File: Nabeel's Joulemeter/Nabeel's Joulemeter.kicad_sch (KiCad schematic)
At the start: 54 parts, among them J1 430450200, J3 22035035, J4 22035035, J5 430450200, U1 INA181A1QDBVRQ1, U2 PADS131M04QPWRQ1, U3 UA78M05QDCYRG4Q1, U4 MCP6286T-E/OT

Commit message: LFG BOARD DONE FR
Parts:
- added C12, C13: 4.7uF, 100V, SMV_Passives:CAP_C2220C_2S_KEM, symbol SMV_Custom:C2220C475M1R2C7186
- TP1, TP10, TP11, TP12, TP13, TP14, TP15, TP16, TP17, TP18, TP2, TP3, TP4, TP5, TP6, TP7, TP8, TP9: footprint TestPoint:TestPoint_Pad_D2.0mm -> TestPoint:TestPoint_Pad_D1.0mm
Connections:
- net +12V: now also C12.1
- net GND: now also C12.2, C13.2
- net SHUNT_TO_LOAD: now also C13.1
- net CAN_H renamed CAN_P
- net CAN_L renamed CAN_N

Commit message: made some changes
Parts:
- added H1, H2, H3, H4: MountingHole, MountingHole:MountingHole_5mm, symbol Mechanical:MountingHole

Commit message: almost final
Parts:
- H1, H2, H3, H4: footprint MountingHole:MountingHole_5mm -> MountingHole:MountingHole_3.2mm_M3
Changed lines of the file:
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@@
 			)
 		)
-		(property "Footprint" "MountingHole:MountingHole_5mm"
+		(property "Footprint" "MountingHole:MountingHole_3.2mm_M3"
 			(at 175.26 24.13 0)
 			(effects
@@
 			)
 		)
-		(property "Footprint" "MountingHole:MountingHole_5mm"
+		(property "Footprint" "MountingHole:MountingHole_3.2mm_M3"
 			(at 185.42 40.64 0)
 			(effects
@@
 			)
 		)
-		(property "Footprint" "MountingHole:MountingHole_5mm"
+		(property "Footprint" "MountingHole:MountingHole_3.2mm_M3"
 			(at 180.2881 33.9955 0)
 			(effects
@@
 			)
 		)
-		(property "Footprint" "MountingHole:MountingHole_5mm"
+		(property "Footprint" "MountingHole:MountingHole_3.2mm_M3"
 			(at 190.5 46.99 0)
 			(effects

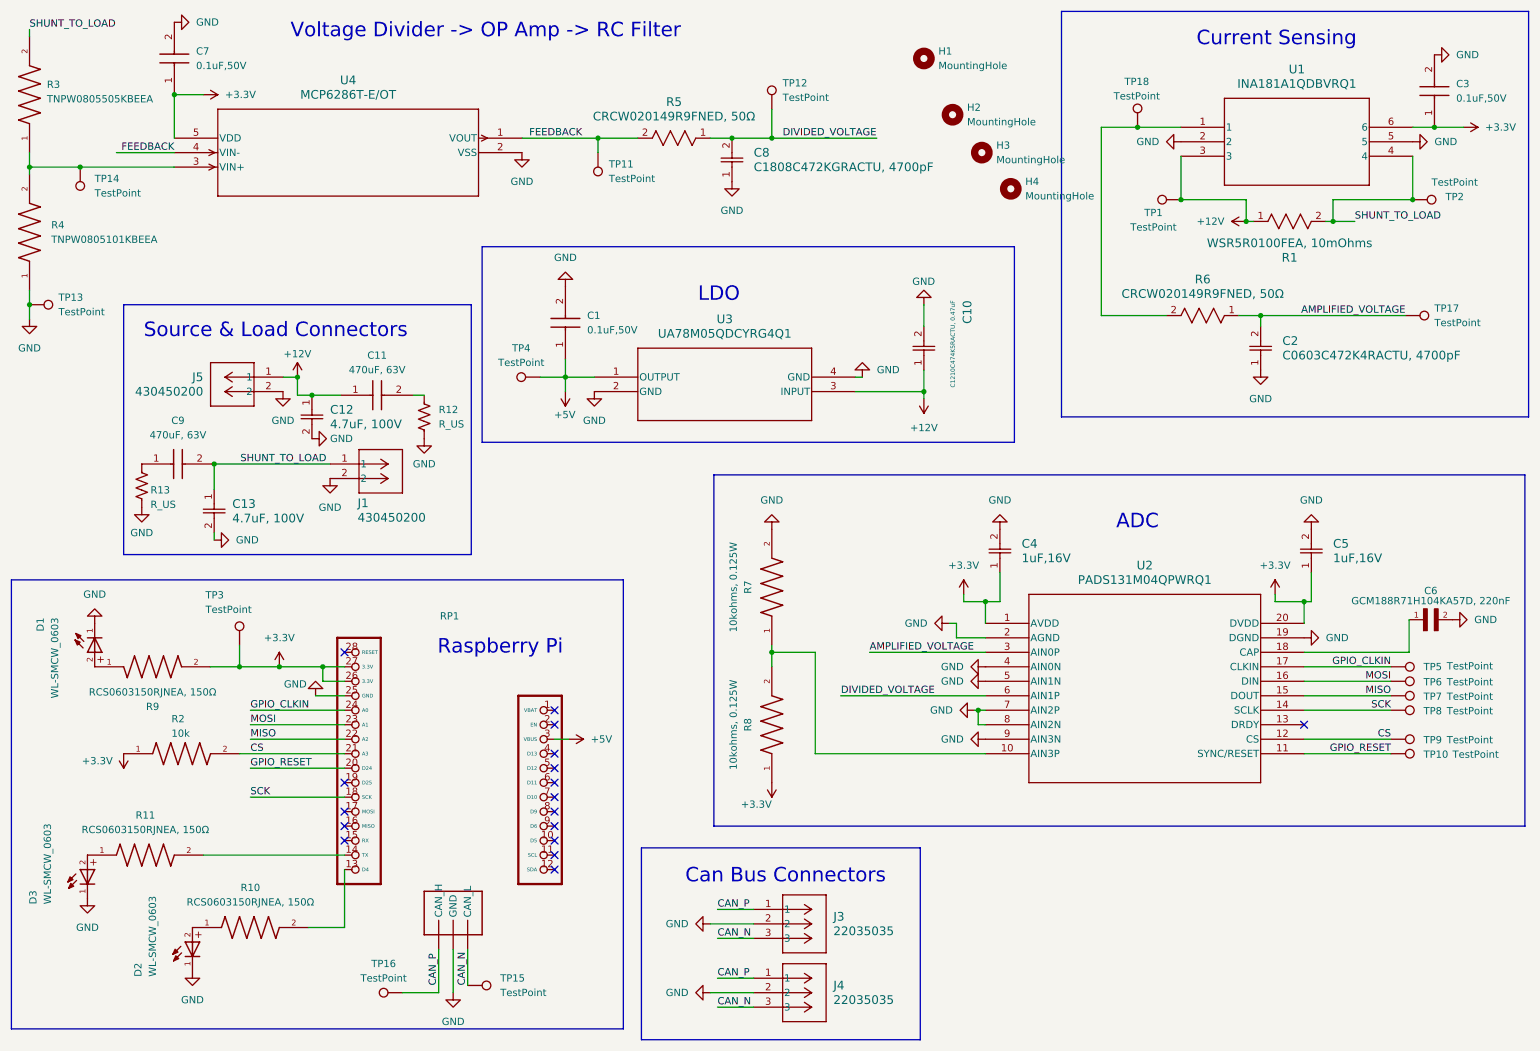
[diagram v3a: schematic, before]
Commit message: Replaced several componentes
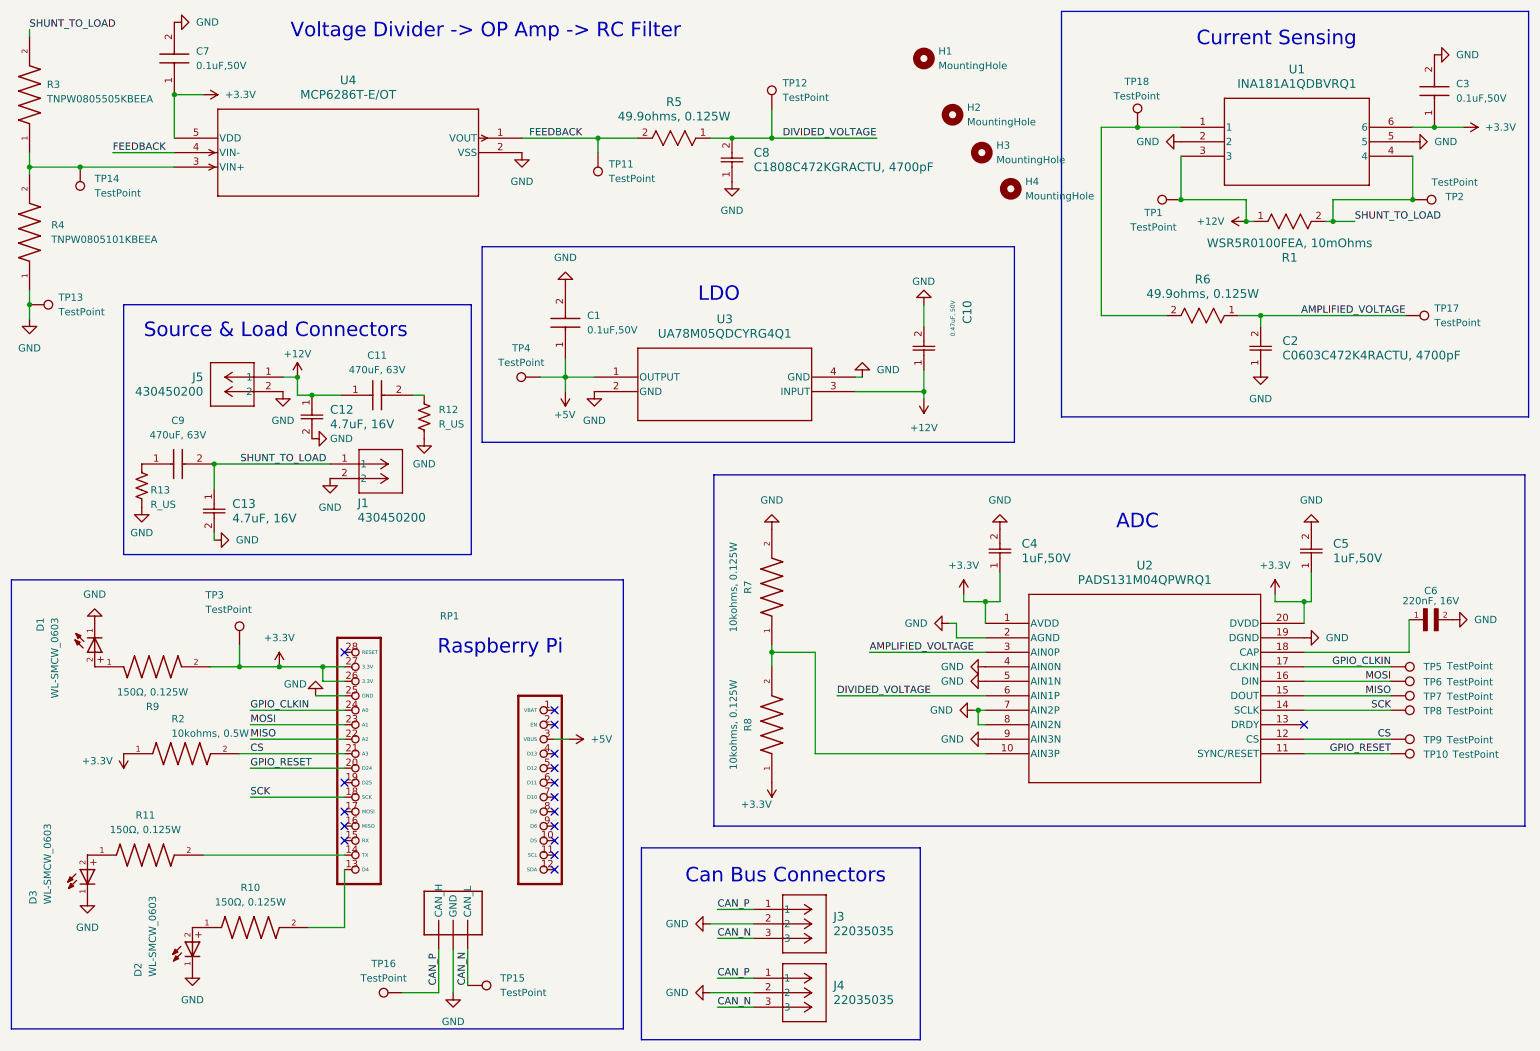
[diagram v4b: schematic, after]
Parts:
- C10: value C1210C474K5RACTU, 0.47uF -> 0.47uF, 50V
- C12, C13: value 4.7uF, 100V -> 4.7uF, 16V; footprint SMV_Passives:CAP_C2220C_2S_KEM -> SMV_Passives:RES_TNPW0805_VIS
- C4, C5: value 1uF,16V -> 1uF,50V
- C6: value GCM188R71H104KA57D, 220nF -> 220nF, 16V
- R10, R11, R9: value RCS0603150RJNEA, 150Ω -> 150Ω, 0.125W
- R2: value 10k -> 10kohms, 0.5W
- R5, R6: value CRCW020149R9FNED, 50Ω -> 49.9ohms, 0.125W
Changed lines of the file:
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@@
 	(wire
 		(pts
-			(xy 33.655 40.64) (xy 43.815 40.64)
-		)
-		(stroke
-			(width 0)
-			(type default)
-		)
-	)
-	(wire
-		(pts
 			(xy 245.745 52.705) (xy 247.015 52.705)
 		)
@@
 	(wire
 		(pts
+			(xy 160.02 135.89) (xy 186.055 135.89)
+		)
+		(stroke
+			(width 0)
+			(type default)
+		)
+	)
+	(wire
+		(pts
 			(xy 145.415 175.895) (xy 137.795 175.895)
 		)
@@
 	(wire
 		(pts
-			(xy 160.655 135.89) (xy 186.055 135.89)
-		)
-		(stroke
-			(width 0)
-			(type default)
-		)
-	)
-	(wire
-		(pts
 			(xy 230.505 69.215) (xy 234.315 69.215)
 		)
@@
 	(wire
 		(pts
+			(xy 33.02 40.64) (xy 43.815 40.64)
+		)
+		(stroke
+			(width 0)
+			(type default)
+		)
+	)
+	(wire
+		(pts
 			(xy 182.245 119.38) (xy 182.245 118.11)
 		)
@@
 	)
 	(label "FEEDBACK"
-		(at 43.815 40.64 180)
+		(at 33.02 40.64 0)
 		(fields_autoplaced yes)
 		(effects
@@
 				(size 1.27 1.27)
 			)
-			(justify right bottom)
+			(justify left bottom)
 		)
 	)
@@
 	)
 	(label "DIVIDED_VOLTAGE"
-		(at 177.165 135.89 180)
+		(at 160.02 135.89 0)
 		(fields_autoplaced yes)
 		(effects
@@
 				(size 1.27 1.27)
 			)
-			(justify right bottom)
+			(justify left bottom)
 		)
 	)
@@
 			)
 		)
-		(property "Value" "GCM188R71H104KA57D, 220nF"
+		(property "Value" "220nF, 16V"
 			(at 264.16 119.253 0)
 			(effects
@@
 			)
 		)
-		(property "Datasheet" ""
+		(property "Datasheet" "C0805C224K5RACAUTO"
 			(at 262.89 122.555 0)
 			(effects
@@
 			)
 		)
-		(property "Description" ""
+		(property "Description" "C129652"
 			(at 262.89 122.555 0)
 			(effects
@@
 			)
 		)
-		(property "Datasheet" "https://content.kemet.com/datasheets/KEM_C1002_X7R_SMD.pdf"
+		(property "Datasheet" "C0805F104K5RACAUTO"
 			(at 460.985 27.305 0)
 			(effects
@@
 			)
 		)
-		(property "Description" "SMD Comm X7R, Ceramic, 0.1 uF, 10%, 50 VDC, 125 VDC, 125C, -55C, X7R, SMD, MLCC, Temperature Stable, Class II, 2.5 % , 5 GOhms, 11 mg, 0805, 2mm, 1.25mm, 0.78mm, 0.75mm, 0.5mm, 4000, 78  Weeks, 80"
+		(property "Description" "C141162"
 			(at 264.795 36.195 0)
 			(effects
@@
 			)
 		)
-		(property "Value" "RCS0603150RJNEA, 150Ω"
+		(property "Value" "150Ω, 0.125W"
 			(at 38.735 159.385 0)
 			(effects
@@
 			)
 		)
-		(property "Datasheet" ""
+		(property "Datasheet" "CRCW0805150RFKEA"
 			(at 38.735 163.83 0)
 			(effects
@@
 			)
 		)
-		(property "Description" ""
+		(property "Description" "C844818"
 			(at 38.735 163.83 0)
 			(effects
@@
 			)
 		)
-		(property "Datasheet" "https://content.kemet.com/datasheets/KEM_C1002_X7R_SMD.pdf"
+		(property "Datasheet" "C0805F104K5RACAUTO"
 			(at 240.005 21.59 0)
 			(effects
@@
 			)
 		)
-		(property "Description" "SMD Comm X7R, Ceramic, 0.1 uF, 10%, 50 VDC, 125 VDC, 125C, -55C, X7R, SMD, MLCC, Temperature Stable, Class II, 2.5 % , 5 GOhms, 11 mg, 0805, 2mm, 1.25mm, 0.78mm, 0.75mm, 0.5mm, 4000, 78  Weeks, 80"
+		(property "Description" "C141162"
 			(at 43.815 30.48 0)
 			(effects
@@
 			)
 		)
-		(property "Value" "1uF,16V"
+		(property "Value" "1uF,50V"
 			(at 247.015 111.7599 90)
 			(effects
@@
 			)
 		)
-		(property "Datasheet" "C0805C105K4RACTU"
+		(property "Datasheet" "C0805X105K5RACAUTO"
 			(at 243.205 114.3 0)
 			(effects
@@
 			)
 		)
-		(property "Description" ""
+		(property "Description" "C3858054"
 			(at 243.205 114.3 0)
 			(effects
@@
 			)
 		)
-		(property "Datasheet" "https://content.kemet.com/datasheets/KEM_C1002_X7R_SMD.pdf"
+		(property "Datasheet" "C0805F104K5RACAUTO"
 			(at 308.585 67.945 0)
 			(effects
@@
 			)
 		)
-		(property "Description" "SMD Comm X7R, Ceramic, 0.1 uF, 10%, 50 VDC, 125 VDC, 125C, -55C, X7R, SMD, MLCC, Temperature Stable, Class II, 2.5 % , 5 GOhms, 11 mg, 0805, 2mm, 1.25mm, 0.78mm, 0.75mm, 0.5mm, 4000, 78  Weeks, 80"
+		(property "Description" "C141162"
 			(at 112.395 76.835 0)
 			(effects
@@
 			)
 		)
-		(property "Value" "C1210C474K5RACTU, 0.47uF"
+		(property "Value" "0.47uF, 50V"
 			(at 180.34 66.548 0)
 			(effects
@@
 			)
 		)
-		(property "Datasheet" "C1210C474K5RACTU"
+		(property "Datasheet" "C0805X474K5RACAUTO"
 			(at 175.26 78.74 0)
 			(effects
@@
 			)
 		)
-		(property "Description" ""
+		(property "Description" "C2173145"
 			(at 175.26 78.74 0)
 			(effects
@@
 			)
 		)
-		(property "Value" "1uF,16V"
+		(property "Value" "1uF,50V"
 			(at 192.405 111.7599 90)
 			(effects
@@
 			)
 		)
-		(property "Datasheet" "C0805C105K4RACTU"
+		(property "Datasheet" "C0805X105K5RACAUTO"
 			(at 188.595 114.3 0)
 			(effects
@@
 			)
 		)
-		(property "Description" ""
+		(property "Description" "C3858054"
 			(at 188.595 114.3 0)
 			(effects
@@
 			)
 		)
-		(property "Value" "RCS0603150RJNEA, 150Ω"
+		(property "Value" "150Ω, 0.125W"
 			(at 57.15 172.085 0)
 			(effects
@@
 			)
 		)
-		(property "Datasheet" ""
+		(property "Datasheet" "CRCW0805150RFKEA"
 			(at 57.15 176.53 0)
 			(effects
@@
 			)
 		)
-		(property "Description" ""
+		(property "Description" "C844818"
 			(at 57.15 176.53 0)
 			(effects
@@
 			)
 		)
-		(property "Value" "10k"
+		(property "Value" "10kohms, 0.5W"
 			(at 43.307 142.494 0)
 			(effects
@@
 			)
 		)
-		(property "Datasheet" ""
+		(property "Datasheet" "CRCW080510K0FKEAHP"
 			(at 45.085 146.05 0)
 			(effects
@@
 			)
 		)
-		(property "Description" ""
+		(property "Description" "C313823"
 			(at 45.085 146.05 0)
 			(effects
@@
 			)
 		)
-		(property "Value" "CRCW020149R9FNED, 50Ω"
+		(property "Value" "49.9ohms, 0.125W"
 			(at 131.445 34.29 0)
 			(effects
@@
 			)
 		)
-		(property "Datasheet" "CRCW020149R9FNED"
+		(property "Datasheet" "CRCW080549R9FKEA"
 			(at 119.253 46.736 0)
 			(effects
@@
 			)
 		)
-		(property "Description" ""
+		(property "Description" "C844847"
 			(at 125.095 38.1 0)
 			(effects
@@
 			)
 		)
-		(property "Datasheet" ""
+		(property "Datasheet" "CRCW080510K0FKEAHP"
 			(at 148.59 140.97 0)
 			(effects
@@
 			)
 		)
-		(property "Description" ""
+		(property "Description" "C313823"
 			(at 148.59 140.97 0)
 			(effects
@@
 			)
 		)
-		(property "Value" "4.7uF, 100V"
+		(property "Value" "4.7uF, 16V"
 			(at 53.975 104.7749 90)
 			(effects
@@
 			)
 		)
-		(property "Footprint" "SMV_Passives:CAP_C2220C_2S_KEM"
+		(property "Footprint" "SMV_Passives:RES_TNPW0805_VIS"
 			(at 50.8 99.695 0)
 			(effects
@@
 			)
 		)
-		(property "Datasheet" "C2220C475M1R2C7186"
+		(property "Datasheet" "C0805C475K4RACAUTO"
 			(at 50.8 99.695 0)
 			(effects
@@
 			)
 		)
-		(property "Description" ""
+		(property "Description" "C599948"
 			(at 50.8 99.695 0)
 			(effects
@@
 			)
 		)
-		(property "Value" "RCS0603150RJNEA, 150Ω"
+		(property "Value" "150Ω, 0.125W"
 			(at 40.005 135.255 0)
 			(effects
@@
 			)
 		)
-		(property "Datasheet" ""
+		(property "Datasheet" "CRCW0805150RFKEA"
 			(at 40.005 130.81 0)
 			(effects
@@
 			)
 		)
-		(property "Description" ""
+		(property "Description" "C844818"
 			(at 40.005 130.81 0)
 			(effects
@@
 			)
 		)
-		(property "Value" "4.7uF, 100V"
+		(property "Value" "4.7uF, 16V"
 			(at 71.12 88.2649 90)
 			(effects
@@
 			)
 		)
-		(property "Footprint" "SMV_Passives:CAP_C2220C_2S_KEM"
+		(property "Footprint" "SMV_Passives:RES_TNPW0805_VIS"
 			(at 67.945 83.185 0)
 			(effects
@@
 			)
 		)
-		(property "Datasheet" "C2220C475M1R2C7186"
+		(property "Datasheet" "C0805C475K4RACAUTO"
 			(at 67.945 83.185 0)
 			(effects
@@
 			)
 		)
-		(property "Description" ""
+		(property "Description" "C599948"
 			(at 67.945 83.185 0)
 			(effects
@@
 			)
 		)
-		(property "Datasheet" ""
+		(property "Datasheet" "CRCW080510K0FKEAHP"
 			(at 148.59 116.84 0)
 			(effects
@@
 			)
 		)
-		(property "Description" ""
+		(property "Description" "C313823"
 			(at 148.59 116.84 0)
 			(effects
@@
 			)
 		)
-		(property "Value" "CRCW020149R9FNED, 50Ω"
+		(property "Value" "49.9ohms, 0.125W"
 			(at 224.155 65.405 0)
 			(effects
@@
 			)
 		)
-		(property "Datasheet" "CRCW020149R9FNED"
+		(property "Datasheet" "CRCW080549R9FKEA"
 			(at 211.963 77.851 0)
 			(effects
@@
 			)
 		)
-		(property "Description" ""
+		(property "Description" "C844847"
 			(at 217.805 69.215 0)
 			(effects

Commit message: fml
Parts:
- C10: footprint SMV_Passives:CAPC340270_105N_KEM -> SMV_Passives:Cap0805
- C12, C13: value 4.7uF, 16V -> 4.7uF, 100V; footprint SMV_Passives:RES_TNPW0805_VIS -> SMV_Passives:CAPC340180_180N_KEM
- C2: value C0603C472K4RACTU, 4700pF -> 4.7nF
- C6: footprint SMV_Passives:0805RESC2012X60N -> SMV_Passives:Cap0805
- C8: value C1808C472KGRACTU, 4700pF -> 4.7nF; footprint CAPC520220_215N_KEM -> SMV_Passives:CAPC17595_87N_KEM
- R3: value TNPW0805505KBEEA -> 51kohms
- R4: value TNPW0805101KBEEA -> 10kohms
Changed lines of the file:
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@@
 			)
 		)
-		(property "Footprint" "SMV_Passives:0805RESC2012X60N"
+		(property "Footprint" "SMV_Passives:Cap0805"
 			(at 262.89 122.555 0)
 			(effects
@@
 			)
 		)
-		(property "Value" "TNPW0805505KBEEA"
+		(property "Value" "51kohms"
 			(at 21.463 31.242 90)
 			(effects
@@
 			)
 		)
-		(property "Datasheet" ""
+		(property "Datasheet" "CRCW060351K0FKEA"
 			(at 18.415 30.48 0)
 			(effects
@@
 			)
 		)
-		(property "Description" ""
+		(property "Description" "C844796"
 			(at 18.415 30.48 0)
 			(effects
@@
 			)
 		)
-		(property "Description" ""
+		(property "Description" "C2058094"
 			(at 220.345 36.195 0)
 			(effects
@@
 			)
 		)
-		(property "Description" "SMD Comm C0G, Ceramic, 1000 pF, 10%, 50 VDC, 125 VDC, 125C, -55C, C0G, SMD, MLCC, Ultra-Stable, Low Loss, Class I, 0.1 % , 100 GOhms, 11 mg, 0805, 2mm, 1.25mm, 0.78mm, 0.75mm, 0.5mm, 4000, 78  Weeks, 120"
+		(property "Description" ""
 			(at 73.025 83.185 0)
 			(effects
@@
 			)
 		)
-		(property "Footprint" "SMV_Passives:CAPC340270_105N_KEM"
+		(property "Footprint" "SMV_Passives:Cap0805"
 			(at 175.26 78.74 0)
 			(effects
@@
 			)
 		)
-		(property "Description" ""
+		(property "Description" "C499500"
 			(at 233.045 52.705 0)
 			(effects
@@
 			)
 		)
-		(property "Value" "TNPW0805101KBEEA"
+		(property "Value" "10kohms"
 			(at 22.225 55.8799 90)
 			(effects
@@
 			)
 		)
-		(property "Datasheet" ""
+		(property "Datasheet" "CRCW080510K0FKEAHP"
 			(at 18.415 54.61 0)
 			(effects
@@
 			)
 		)
-		(property "Description" ""
+		(property "Description" "C313823"
 			(at 18.415 54.61 0)
 			(effects
@@
 			)
 		)
-		(property "Description" ""
+		(property "Description" "C2286"
 			(at 46.99 181.61 0)
 			(effects
@@
 			)
 		)
-		(property "Description" ""
+		(property "Description" "C2286"
 			(at 29.845 125.73 0)
 			(effects
@@
 			)
 		)
-		(property "Value" "C0603C472K4RACTU, 4700pF"
+		(property "Value" "4.7nF"
 			(at 238.125 76.1999 90)
 			(effects
@@
 			)
 		)
-		(property "Datasheet" "C0603C472K4RACTU"
+		(property "Datasheet" "C0603C472K5RACAUTO"
 			(at 234.315 78.74 0)
 			(effects
@@
 			)
 		)
-		(property "Description" ""
+		(property "Description" "C141106"
 			(at 234.315 78.74 0)
 			(effects
@@
 			)
 		)
-		(property "Description" "SMD Comm C0G, Ceramic, 1000 pF, 10%, 50 VDC, 125 VDC, 125C, -55C, C0G, SMD, MLCC, Ultra-Stable, Low Loss, Class I, 0.1 % , 100 GOhms, 11 mg, 0805, 2mm, 1.25mm, 0.78mm, 0.75mm, 0.5mm, 4000, 78  Weeks, 120"
+		(property "Description" ""
 			(at 38.1 95.25 0)
 			(effects
@@
 			)
 		)
-		(property "Description" ""
+		(property "Description" "C485570"
 			(at 117.475 80.01 0)
 			(effects
@@
 			)
 		)
-		(property "Description" ""
+		(property "Description" "C2286"
 			(at 28.575 168.91 0)
 			(effects
@@
 			)
 		)
-		(property "Value" "4.7uF, 16V"
+		(property "Value" "4.7uF, 100V"
 			(at 53.975 104.7749 90)
 			(effects
@@
 			)
 		)
-		(property "Footprint" "SMV_Passives:RES_TNPW0805_VIS"
+		(property "Footprint" "SMV_Passives:CAPC340180_180N_KEM"
 			(at 50.8 99.695 0)
 			(effects
@@
 			)
 		)
-		(property "Datasheet" "C0805C475K4RACAUTO"
+		(property "Datasheet" "GRM31CC72A475KE11L"
 			(at 50.8 99.695 0)
 			(effects
@@
 			)
 		)
-		(property "Description" "C599948"
+		(property "Description" "C237304"
 			(at 50.8 99.695 0)
 			(effects
@@
 			)
 		)
-		(property "Value" "4.7uF, 16V"
+		(property "Value" "4.7uF, 100V"
 			(at 71.12 88.2649 90)
 			(effects
@@
 			)
 		)
-		(property "Footprint" "SMV_Passives:RES_TNPW0805_VIS"
+		(property "Footprint" "SMV_Passives:CAPC340180_180N_KEM"
 			(at 67.945 83.185 0)
 			(effects
@@
 			)
 		)
-		(property "Datasheet" "C0805C475K4RACAUTO"
+		(property "Datasheet" "GRM31CC72A475KE11L"
 			(at 67.945 83.185 0)
 			(effects
@@
 			)
 		)
-		(property "Description" "C599948"
+		(property "Description" "C237304"
 			(at 67.945 83.185 0)
 			(effects
@@
 			)
 		)
-		(property "Description" ""
+		(property "Description" "C623478"
 			(at 104.775 38.1 0)
 			(effects
@@
 			)
 		)
-		(property "Value" "C1808C472KGRACTU, 4700pF"
+		(property "Value" "4.7nF"
 			(at 145.415 43.1799 90)
 			(effects
@@
 			)
 		)
-		(property "Footprint" "CAPC520220_215N_KEM"
+		(property "Footprint" "SMV_Passives:CAPC17595_87N_KEM"
 			(at 141.605 45.72 0)
 			(effects
@@
 			)
 		)
-		(property "Datasheet" "C1808C472KGRACTU"
+		(property "Datasheet" "C0603C472K5RACAUTO"
 			(at 141.605 45.72 0)
 			(effects
@@
 			)
 		)
-		(property "Description" ""
+		(property "Description" "C141106"
 			(at 141.605 45.72 0)
 			(effects
